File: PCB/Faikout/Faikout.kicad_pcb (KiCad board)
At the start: 2 copper layers, 70 x 70 mm, 44 parts, among them J1 S21, J2 TC2030-USB-NL, J3 Reset, Q1 BSS138PS, U4 ESP32-S3-MINI-1, U5 TPS62933

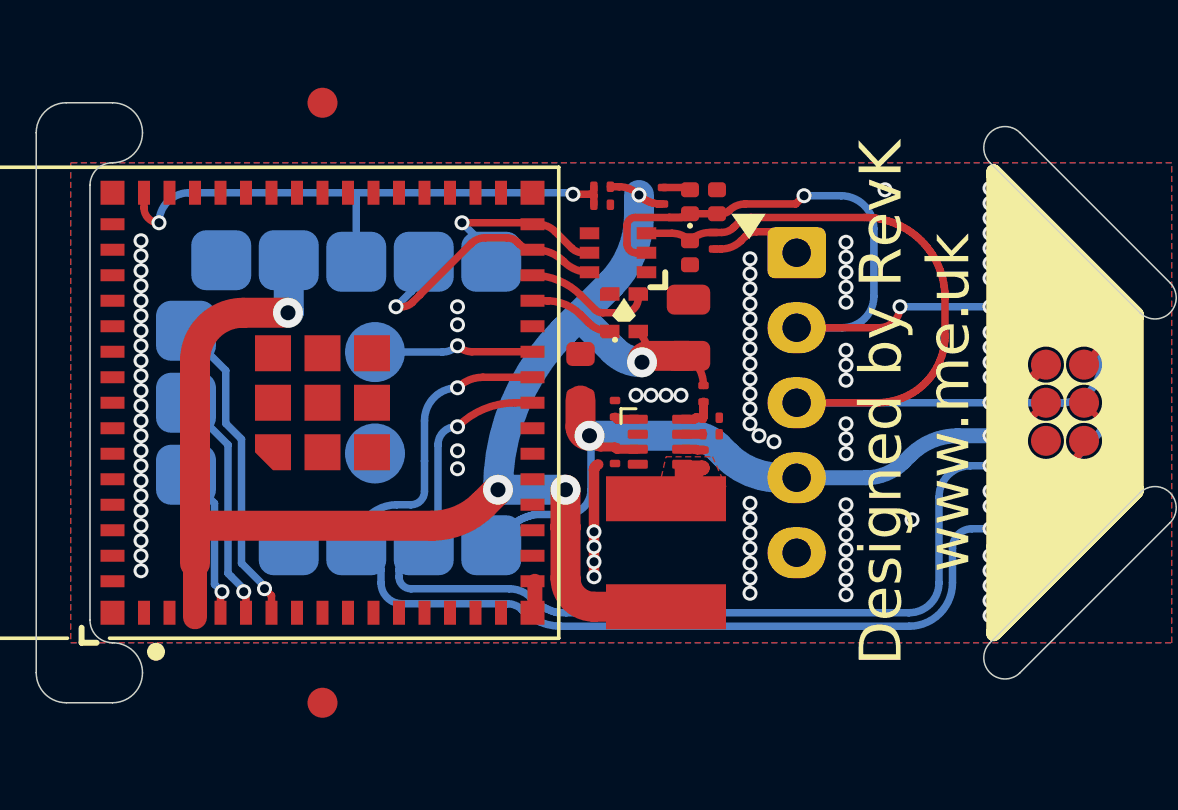
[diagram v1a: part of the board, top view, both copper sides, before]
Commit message: New inductor
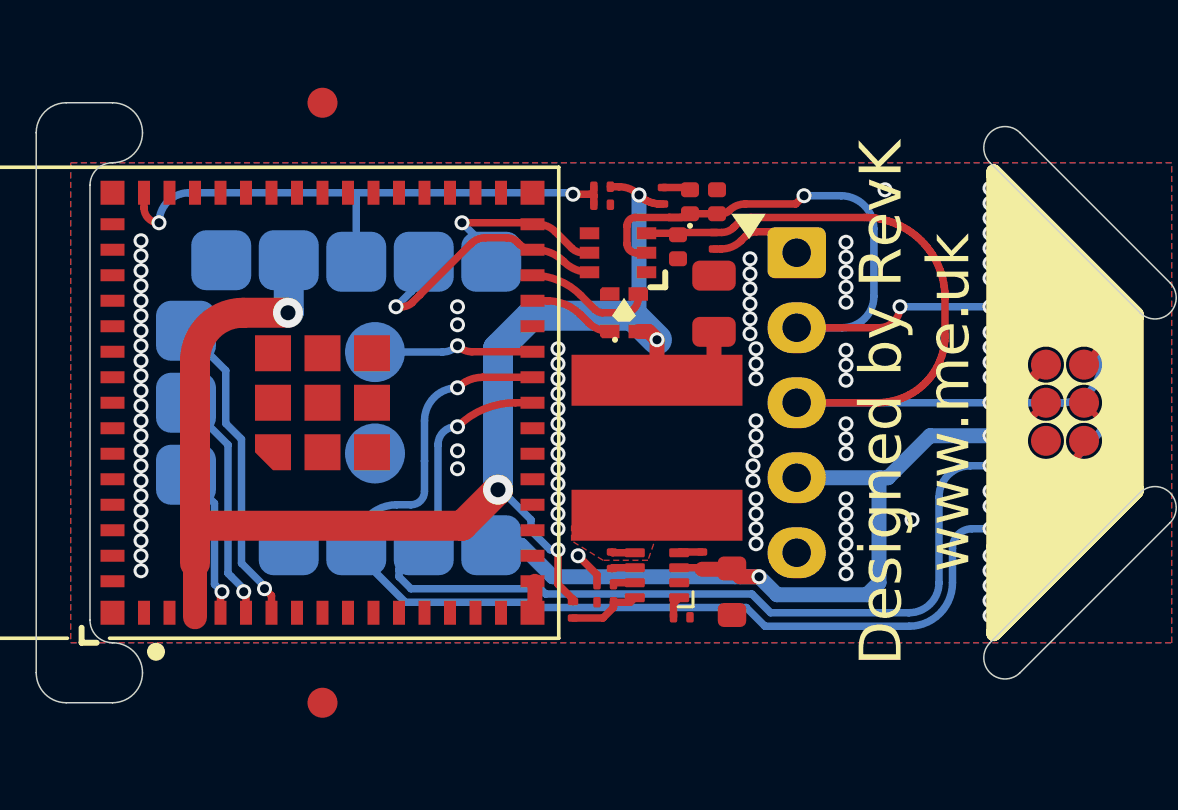
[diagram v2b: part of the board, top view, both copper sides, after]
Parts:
- removed C29: 10uF 35V, RevK:C_0603
- removed C30, C32: 100nF 35V, RevK:C_0201
- removed C31: 33nF, RevK:C_0201
- removed C33: 100uF 6.3V, RevK:C_0805
- removed L13: 4.7uH, RevK:L_5x5
- removed R15: 33k, RevK:R_0201
- removed R16: 30.9k 1%, RevK:R_0201
- removed R17: 10k, RevK:R_0201
- removed U5: TPS62933, RevK:SOT-583-8
- added C1: 10uF 35V, RevK:C_0603, F.Cu at (143.4, 71.3)
- added C2: 100nF 35V, RevK:C_0201, F.Cu at (142.4, 70.2)
- added C3: 33nF, RevK:C_0201, F.Cu at (139.2, 71.0)
- added C4: 100nF 35V, RevK:C_0201, F.Cu at (139.4, 70.2)
- added C5: 100uF 6.3V, RevK:C_0805, F.Cu at (142.8, 61.7)
- added L1: 4.7uH, RevK:L_6x6, F.Cu at (140.9, 66.5)
- added R4: 33k, RevK:R_0201, F.Cu at (141.7, 72.2)
- added R5: 30.9k 1%, RevK:R_0201, F.Cu at (138.1, 71.9)
- added R6: 10k, RevK:R_0201, F.Cu at (139.2, 71.7)
- added U1: TPS62933, RevK:SOT-583-8, F.Cu at (140.9, 70.8)
- moved D2 0.45 mm to (141.6, 59.8)
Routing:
- net DC: track 26.3 -> 30.1 mm
- net SW: track 3.65 -> 0.77 mm
- net GND: track 4.66 -> 3.03 mm, vias 94 -> 96
- net +3.3V: track 53.3 -> 52.0 mm
- net FB: track 1.24 -> 2.48 mm

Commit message: Tweaks
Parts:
- turned FID3 to 180 degrees
